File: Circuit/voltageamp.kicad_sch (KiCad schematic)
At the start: 35 parts, among them U11 INA828D, U12 DG201, U13 OPA2197xD, U14 DG201, U15 OPA2376xxD

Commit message: Output job, Revision Box and reorganise
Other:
- company: Harry and Yuki - EEE3 Instrumentation -> Harry Hill and Yuki Hoshino
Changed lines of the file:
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@@
 	(title_block
 		(title "Voltage Amplifier")
-		(date "2026-03-02")
+		(date "2026-05-02")
 		(rev "1.0")
-		(company "Harry and Yuki - EEE3 Instrumentation")
+		(company "Harry Hill and Yuki Hoshino")
+		(comment 1 "LCR Meter")
 	)
 	(rectangle

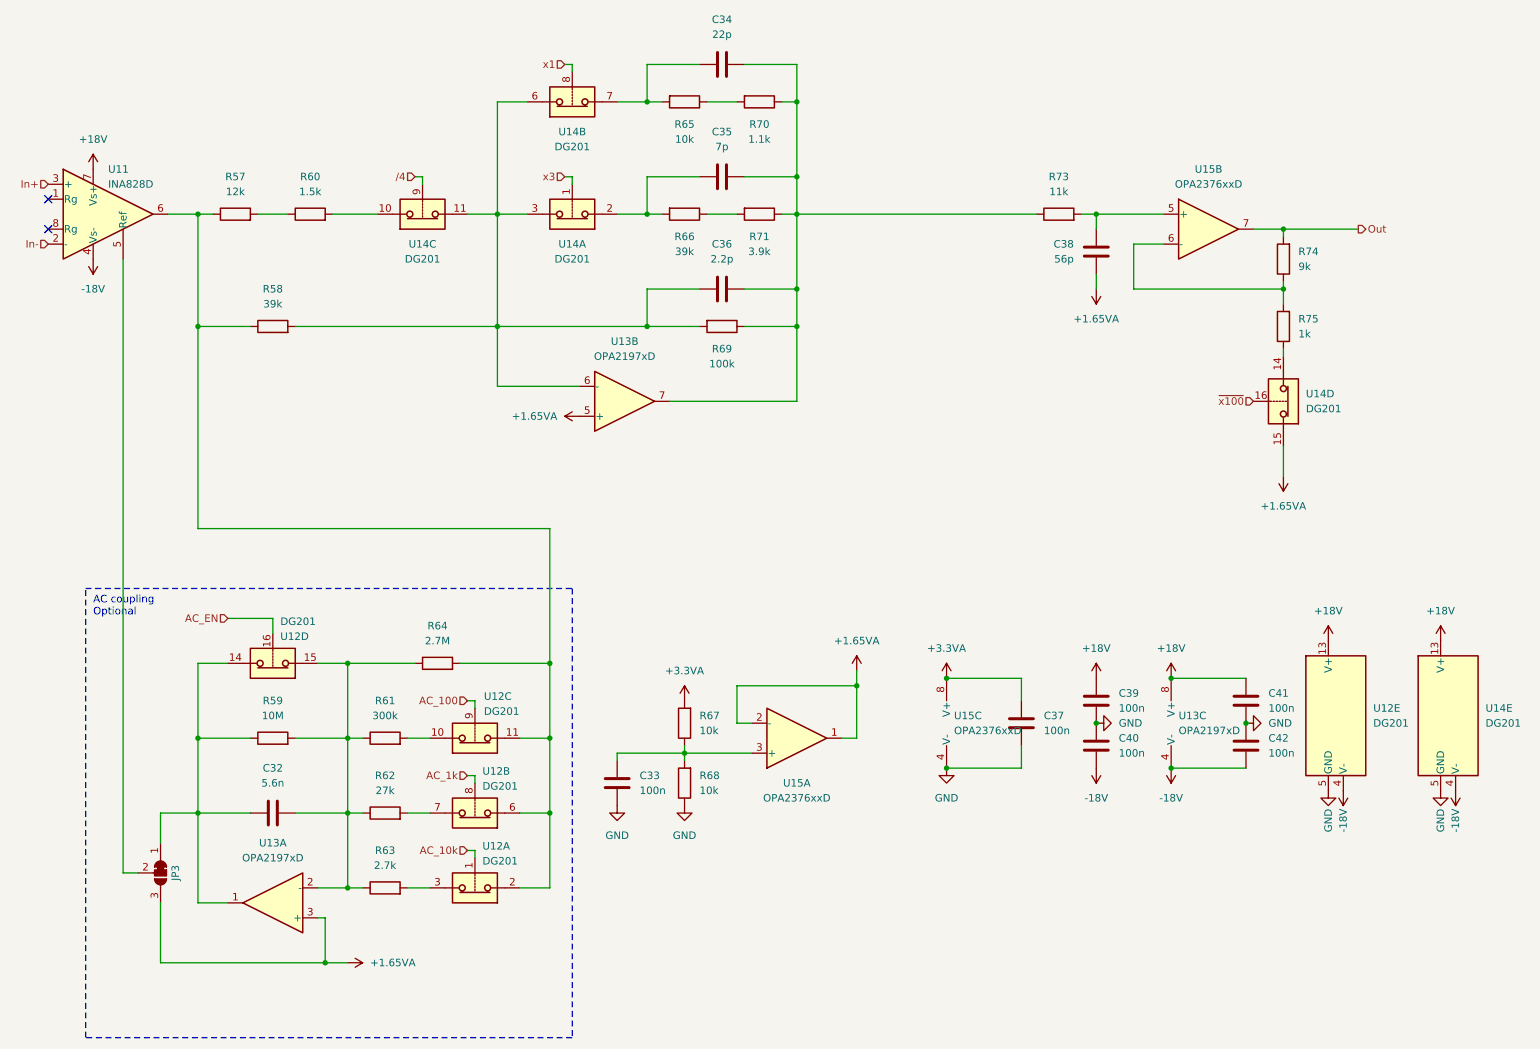
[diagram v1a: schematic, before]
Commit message: Input Protection Second Attempt
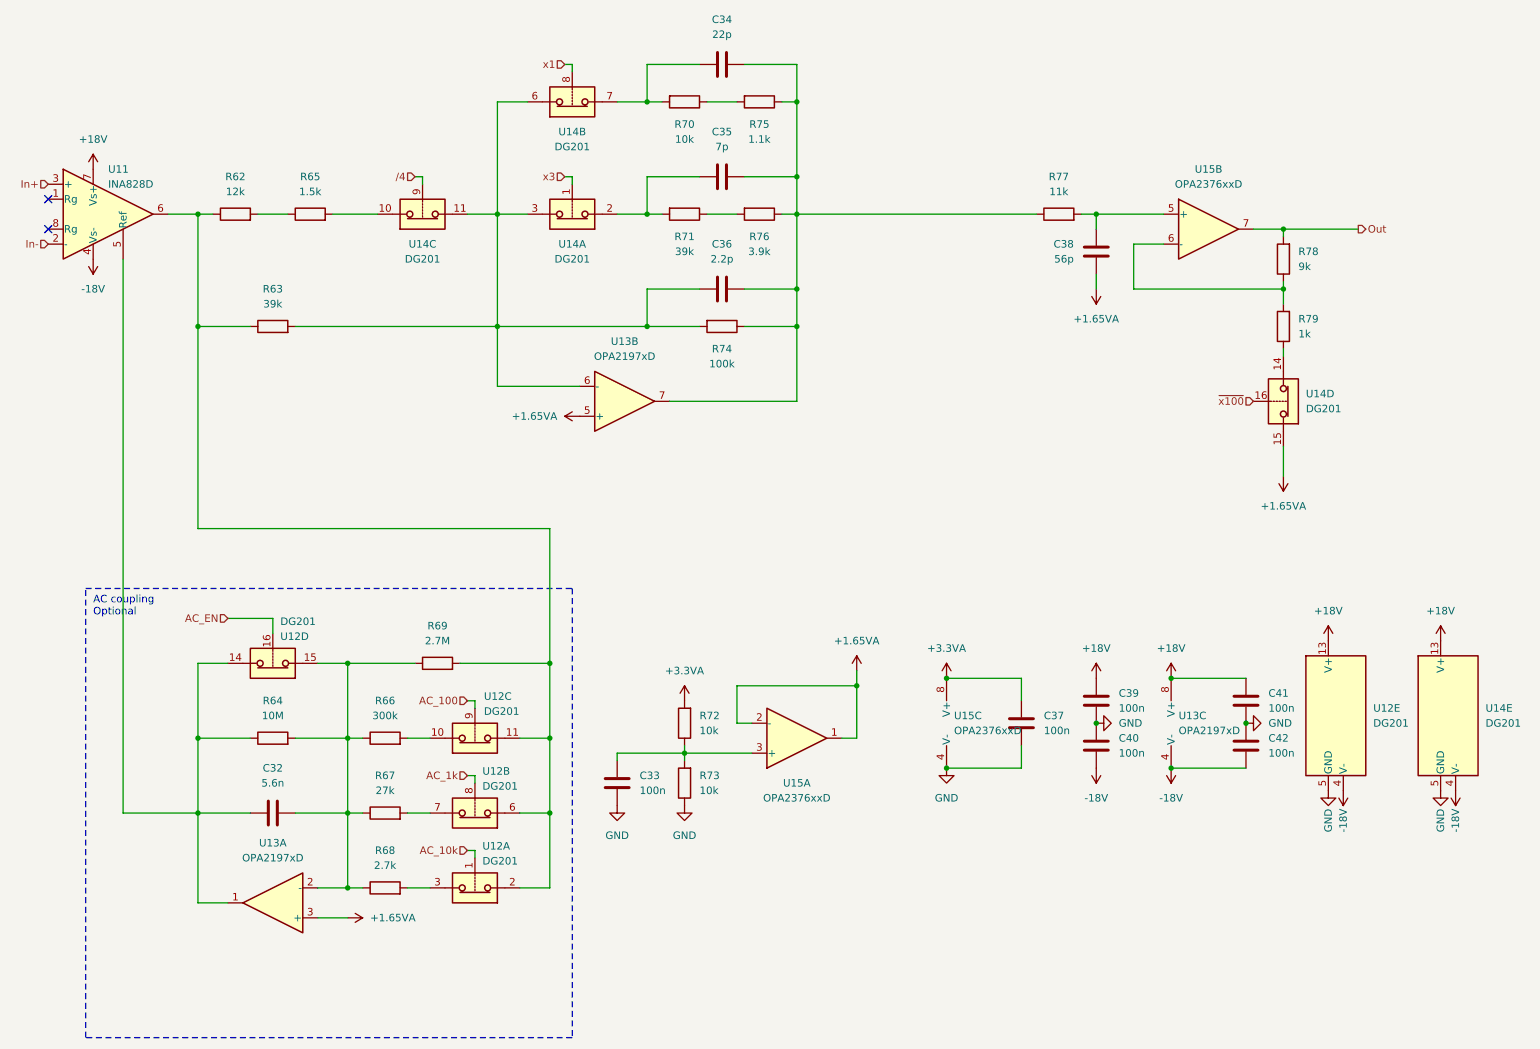
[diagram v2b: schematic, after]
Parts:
- removed JP3: SolderJumper_3_Bridged12, Jumper:SolderJumper-3_P1.3mm_Bridged12_RoundedPad1.0x1.5mm_NumberLabels, symbol Jumper:SolderJumper_3_Bridged12
- renumbered R57 to R62, R58 to R63, R59 to R64, R60 to R65, R61 to R66, R62 to R67, R63 to R68, R64 to R69, R65 to R70, R66 to R71, R67 to R72, R68 to R73, R69 to R74, R70 to R75, R71 to R76, R73 to R77, R74 to R78, R75 to R79
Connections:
- net at C32.1, R64.1, U12.14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: now also U11.5 (Ref)

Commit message: New Resistor Selection Circuit
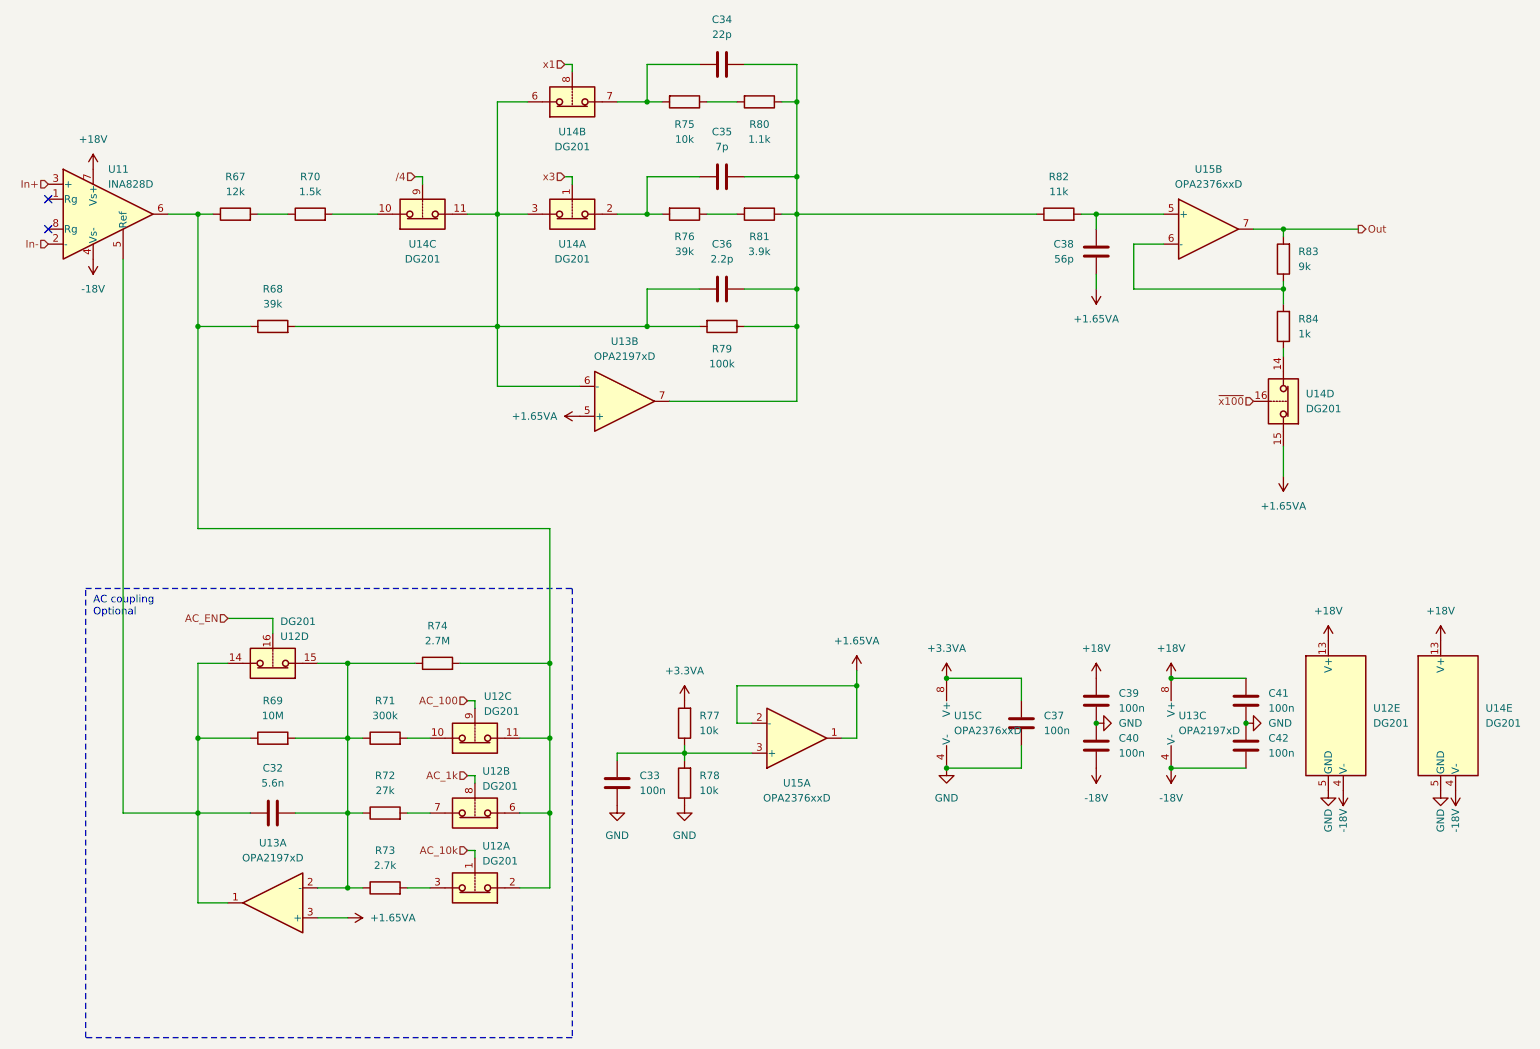
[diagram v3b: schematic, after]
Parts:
- renumbered R62 to R67, R63 to R68, R64 to R69, R65 to R70, R66 to R71, R67 to R72, R68 to R73, R69 to R74, R70 to R75, R71 to R76, R72 to R77, R73 to R78, R74 to R79, R75 to R80, R76 to R81, R77 to R82, R78 to R83, R79 to R84
